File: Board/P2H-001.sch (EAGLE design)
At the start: 28 parts, among them IC1 74LS157N, IC2 LTC485N, IC3 4051N, IC4 74LS07N, IC5 LTC485N

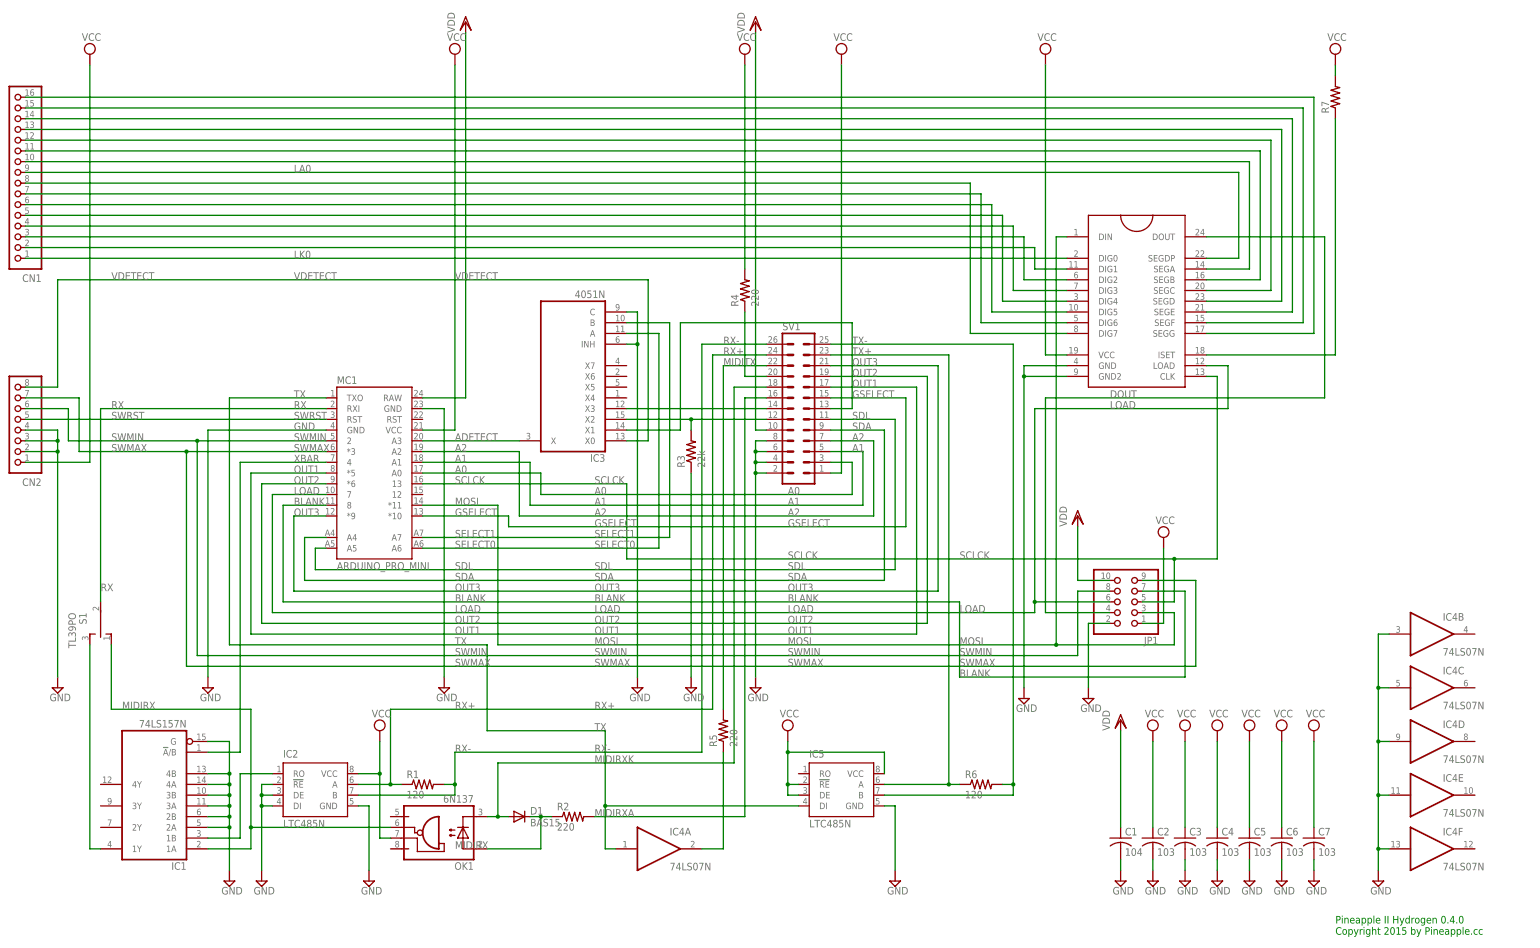
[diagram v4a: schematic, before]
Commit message: New drive port.
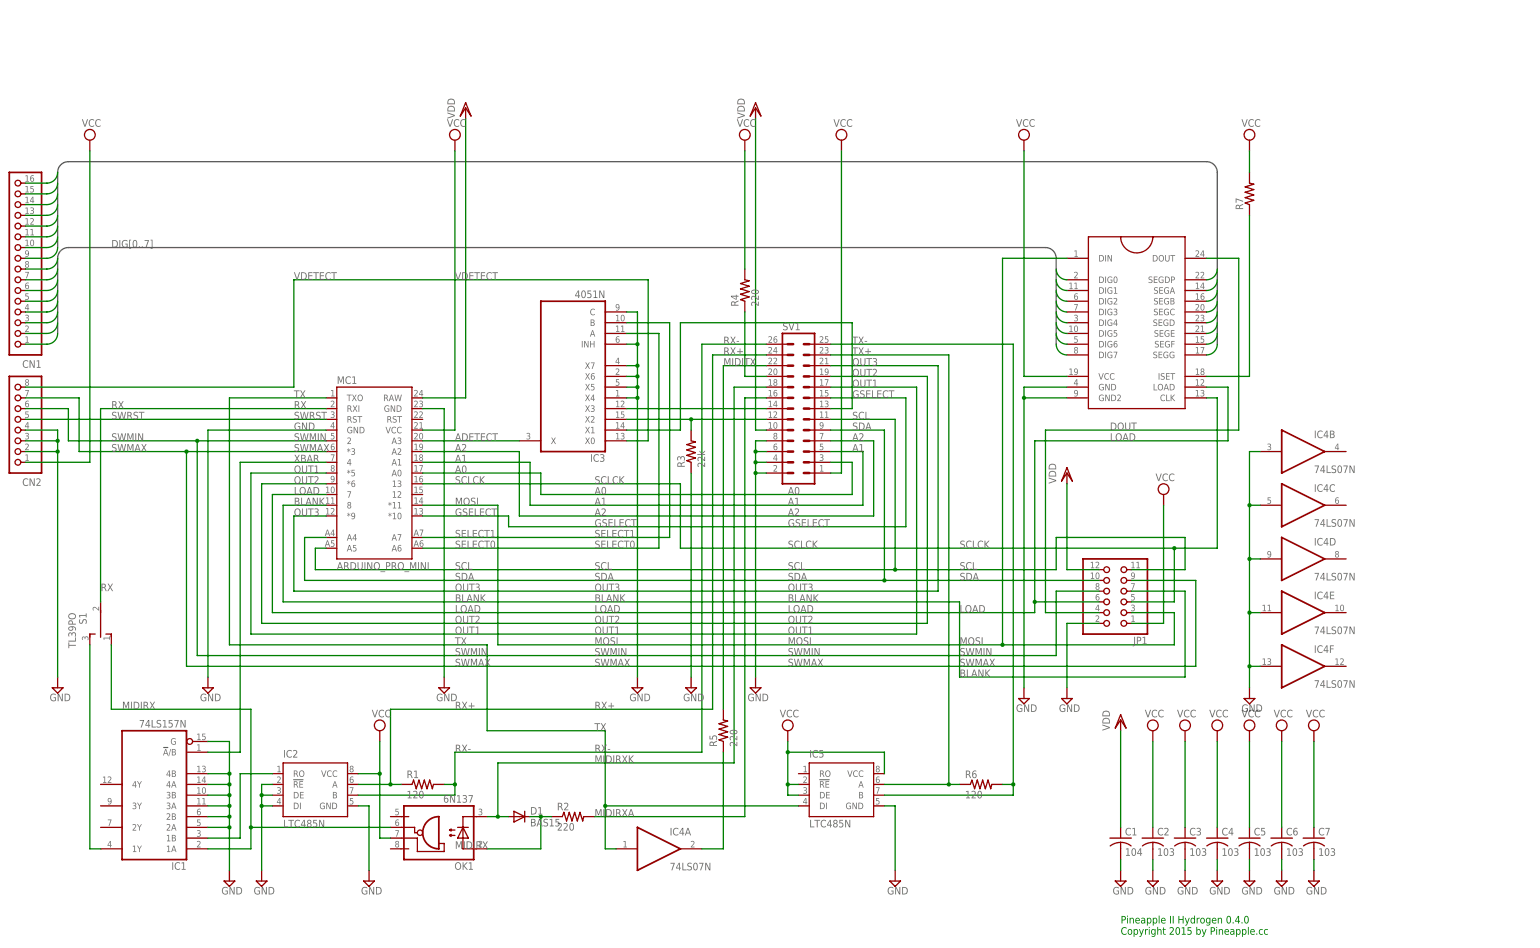
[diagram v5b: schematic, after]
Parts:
- JP1: device pinhead:PINHD-2X5 -> pinhead:PINHD-2X6
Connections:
- net LK0 renamed DIG0
- net N$18 renamed DIG2
- net N$19 renamed DIG3
- net N$22 renamed DIG1
- net N$24 renamed DIG4
- net N$25 renamed DIG5
- net N$26 renamed DIG6
- net N$27 renamed DIG7
- removed net LA0: CN1.9, MC2.SEGDP
- removed net N$29: CN1.10, MC2.SEGA
- removed net N$30: CN1.11, MC2.SEGB
- removed net N$31: CN1.12, MC2.SEGC
- removed net N$32: CN1.13, MC2.SEGD
- removed net N$33: CN1.14, MC2.SEGE
- removed net N$34: CN1.15, MC2.SEGF
- removed net N$35: CN1.16, MC2.SEGG
- removed net SDL: MC1.A5, SV1.11
- new net SCL: JP1.11, MC1.A5, SV1.11
- new net SEG0: CN1.9, MC2.SEGG
- new net SEG1: CN1.10, MC2.SEGF
- new net SEG2: CN1.11, MC2.SEGE
- new net SEG3: CN1.12, MC2.SEGD
- new net SEG4: CN1.13, MC2.SEGC
- new net SEG5: CN1.14, MC2.SEGB
- new net SEG6: CN1.15, MC2.SEGA
- new net SEG7: CN1.16, MC2.SEGDP
- net GND: now also IC3A.X4, IC3A.X5, IC3A.X6, IC3A.X7
- net SDA: now also JP1.10
- net VDD: now also JP1.12; no longer JP1.10
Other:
- moved on the sheet: CN1, IC4B, IC4C, IC4D, IC4E, IC4F, R7

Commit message: Updating...
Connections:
- net RX+: now also SV1.23; no longer SV1.24
- net RX-: now also SV1.24; no longer SV1.26
- net TX+: now also SV1.25; no longer SV1.23
- net TX-: now also SV1.26; no longer SV1.25
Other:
- moved on the sheet: R4
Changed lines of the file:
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@@
 <instances>
 <instance part="SUPPLY1" gate="GND" x="20.32" y="-22.86"/>
-<instance part="R4" gate="G$1" x="182.88" y="71.12" rot="R90"/>
+<instance part="R4" gate="G$1" x="182.88" y="73.66" rot="R90"/>
 <instance part="R5" gate="G$1" x="177.8" y="-33.02" rot="R90"/>
 <instance part="R2" gate="G$1" x="142.24" y="-53.34"/>
@@
 <pinref part="SUPPLY13" gate="G$1" pin="VCC"/>
 <pinref part="R4" gate="G$1" pin="2"/>
-<wire x1="182.88" y1="104.14" x2="182.88" y2="76.2" width="0.1524" layer="91"/>
+<wire x1="182.88" y1="104.14" x2="182.88" y2="78.74" width="0.1524" layer="91"/>
 </segment>
 <segment>
@@
 <wire x1="111.76" y1="-45.72" x2="114.3" y2="-45.72" width="0.1524" layer="91"/>
 <junction x="114.3" y="-45.72"/>
-<pinref part="SV1" gate="1" pin="26"/>
-<wire x1="187.96" y1="58.42" x2="172.72" y2="58.42" width="0.1524" layer="91"/>
-<wire x1="172.72" y1="58.42" x2="172.72" y2="-38.1" width="0.1524" layer="91"/>
+<wire x1="172.72" y1="55.88" x2="172.72" y2="-38.1" width="0.1524" layer="91"/>
 <wire x1="172.72" y1="-38.1" x2="114.3" y2="-38.1" width="0.1524" layer="91"/>
 <wire x1="114.3" y1="-38.1" x2="114.3" y2="-45.72" width="0.1524" layer="91"/>
 <label x="114.3" y="-38.1" size="1.778" layer="95"/>
 <label x="147.32" y="-38.1" size="1.778" layer="95"/>
-<label x="177.8" y="58.42" size="1.778" layer="95"/>
+<pinref part="SV1" gate="1" pin="24"/>
+<wire x1="172.72" y1="55.88" x2="187.96" y2="55.88" width="0.1524" layer="91"/>
+<label x="180.34" y="55.88" size="1.778" layer="95"/>
 </segment>
 </net>
@@
 <wire x1="91.44" y1="-45.72" x2="99.06" y2="-45.72" width="0.1524" layer="91"/>
 <wire x1="99.06" y1="-27.94" x2="99.06" y2="-45.72" width="0.1524" layer="91"/>
-<pinref part="SV1" gate="1" pin="24"/>
-<wire x1="187.96" y1="55.88" x2="175.26" y2="55.88" width="0.1524" layer="91"/>
-<wire x1="175.26" y1="55.88" x2="175.26" y2="-27.94" width="0.1524" layer="91"/>
-<wire x1="175.26" y1="-27.94" x2="99.06" y2="-27.94" width="0.1524" layer="91"/>
+<wire x1="233.68" y1="55.88" x2="233.68" y2="-27.94" width="0.1524" layer="91"/>
+<wire x1="233.68" y1="-27.94" x2="99.06" y2="-27.94" width="0.1524" layer="91"/>
 <pinref part="R1" gate="G$1" pin="1"/>
 <wire x1="101.6" y1="-45.72" x2="99.06" y2="-45.72" width="0.1524" layer="91"/>
@@
 <label x="147.32" y="-27.94" size="1.778" layer="95"/>
 <label x="114.3" y="-27.94" size="1.778" layer="95"/>
-<label x="177.8" y="55.88" size="1.778" layer="95"/>
+<pinref part="SV1" gate="1" pin="23"/>
+<wire x1="233.68" y1="55.88" x2="203.2" y2="55.88" width="0.1524" layer="91"/>
+<label x="208.28" y="55.88" size="1.778" layer="95"/>
 </segment>
 </net>
@@
 <pinref part="R6" gate="G$1" pin="1"/>
 <wire x1="215.9" y1="-45.72" x2="231.14" y2="-45.72" width="0.1524" layer="91"/>
-<pinref part="SV1" gate="1" pin="23"/>
 <wire x1="231.14" y1="-45.72" x2="233.68" y2="-45.72" width="0.1524" layer="91"/>
-<wire x1="203.2" y1="55.88" x2="231.14" y2="55.88" width="0.1524" layer="91"/>
-<wire x1="231.14" y1="55.88" x2="231.14" y2="-45.72" width="0.1524" layer="91"/>
+<wire x1="231.14" y1="58.42" x2="231.14" y2="-45.72" width="0.1524" layer="91"/>
 <junction x="231.14" y="-45.72"/>
-<label x="208.28" y="55.88" size="1.778" layer="95"/>
+<pinref part="SV1" gate="1" pin="25"/>
+<wire x1="231.14" y1="58.42" x2="203.2" y2="58.42" width="0.1524" layer="91"/>
+<label x="208.28" y="58.42" size="1.778" layer="95"/>
 </segment>
 </net>
@@
 <wire x1="246.38" y1="-48.26" x2="246.38" y2="-45.72" width="0.1524" layer="91"/>
 <wire x1="246.38" y1="-45.72" x2="243.84" y2="-45.72" width="0.1524" layer="91"/>
-<pinref part="SV1" gate="1" pin="25"/>
-<wire x1="203.2" y1="58.42" x2="246.38" y2="58.42" width="0.1524" layer="91"/>
-<wire x1="246.38" y1="58.42" x2="246.38" y2="-45.72" width="0.1524" layer="91"/>
+<wire x1="246.38" y1="66.04" x2="246.38" y2="-45.72" width="0.1524" layer="91"/>
 <junction x="246.38" y="-45.72"/>
-<label x="208.28" y="58.42" size="1.778" layer="95"/>
+<wire x1="246.38" y1="66.04" x2="180.34" y2="66.04" width="0.1524" layer="91"/>
+<wire x1="180.34" y1="66.04" x2="180.34" y2="58.42" width="0.1524" layer="91"/>
+<pinref part="SV1" gate="1" pin="26"/>
+<wire x1="180.34" y1="58.42" x2="187.96" y2="58.42" width="0.1524" layer="91"/>
+<label x="180.34" y="58.42" size="1.778" layer="95"/>
 </segment>
 </net>
@@
 <wire x1="83.82" y1="20.32" x2="73.66" y2="20.32" width="0.1524" layer="91"/>
 <wire x1="73.66" y1="20.32" x2="73.66" y2="-2.54" width="0.1524" layer="91"/>
-<wire x1="73.66" y1="-2.54" x2="233.68" y2="-2.54" width="0.1524" layer="91"/>
+<wire x1="73.66" y1="-2.54" x2="241.3" y2="-2.54" width="0.1524" layer="91"/>
 <label x="114.3" y="-2.54" size="1.778" layer="95"/>
 <label x="76.2" y="20.32" size="1.778" layer="95"/>
-<wire x1="233.68" y1="-2.54" x2="233.68" y2="-20.32" width="0.1524" layer="91"/>
-<wire x1="233.68" y1="-20.32" x2="287.02" y2="-20.32" width="0.1524" layer="91"/>
+<wire x1="241.3" y1="-2.54" x2="241.3" y2="-20.32" width="0.1524" layer="91"/>
+<wire x1="241.3" y1="-20.32" x2="287.02" y2="-20.32" width="0.1524" layer="91"/>
 <wire x1="287.02" y1="-20.32" x2="287.02" y2="0" width="0.1524" layer="91"/>
 <wire x1="287.02" y1="0" x2="274.32" y2="0" width="0.1524" layer="91"/>
@@
 <segment>
 <pinref part="R4" gate="G$1" pin="1"/>
-<wire x1="182.88" y1="66.04" x2="182.88" y2="50.8" width="0.1524" layer="91"/>
+<wire x1="182.88" y1="68.58" x2="182.88" y2="50.8" width="0.1524" layer="91"/>
 <pinref part="SV1" gate="1" pin="20"/>
 <wire x1="182.88" y1="50.8" x2="187.96" y2="50.8" width="0.1524" layer="91"/>
@@
 <wire x1="177.8" y1="53.34" x2="177.8" y2="-27.94" width="0.1524" layer="91"/>
 <pinref part="R5" gate="G$1" pin="2"/>
-<label x="177.8" y="53.34" size="1.778" layer="95"/>
-</segment>
-</net>
+<label x="180.34" y="53.34" size="1.778" layer="95"/>
+</segment>
+</net>

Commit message: Refine of sch.
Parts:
- removed JP1: (no value), pinhead:PINHD-2X6
- removed MC1: ARDUINO_PRO_MINI, SparkFun-Boards:ARDUINO_PRO_MINI
- removed MC2: MAX7219DIP, SparkFun-DigitalIC:MAX7219DIP
- added U1: ARDUINO_PRO_MINI, SparkFun-Boards:ARDUINO_PRO_MINI
- added U2: MAX7219DIP, SparkFun-DigitalIC:MAX7219DIP
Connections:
- removed net BLANK: JP1.7, MC1.8
- removed net DOUT: JP1.4, MC2.DOUT
- removed net MIDIRXA: R2.2, SV1.16
- removed net MIDIRXK: D1.A, OK1.C, SV1.18
- removed net MIDITX: R5.2, SV1.22
- removed net N$3: IC3A.X1, SV1.13
- removed net N$5: IC3A.X2, R3.2, SV1.12
- removed net N$6: IC3A.X3, SV1.14
- removed net OUT1: MC1.*5, SV1.17
- removed net OUT2: MC1.*6, SV1.19
- removed net OUT3: MC1.*9, SV1.21
- removed net SELECT0: IC3A.A, MC1.A6
- removed net SELECT1: IC3A.B, MC1.A7
- removed net SWRST: CN2.5, MC1.RST
- new net GDETECT: IC3A.X1, SV1.11
- new net L0: SV1.13, U1.*5
- new net L1: SV1.14, U1.*6
- new net L2: SV1.15, U1.*9
- new net MDETECT: IC3A.X2, R3.2, SV1.16
- new net RXA: R2.2, SV1.19
- new net RXK: D1.A, OK1.C, SV1.20
- new net SEL0: IC3A.A, U1.A6
- new net SEL1: IC3A.B, U1.A7
- new net SWMAIN: CN2.3, U1.2
- new net TXSNK: R4.2, SV1.18
- new net XDETECT: IC3A.X3, SV1.22
- net A0: now also U1.A0; no longer MC1.A0
- net A1: now also U1.A1; no longer MC1.A1
- net A2: now also U1.A2; no longer MC1.A2
- net ADETECT: now also U1.A3; no longer MC1.A3
- net DIG0: now also U2.DIG0; no longer MC2.DIG0
- net DIG1: now also U2.DIG1; no longer MC2.DIG1
- net DIG2: now also U2.DIG2; no longer MC2.DIG2
- net DIG3: now also U2.DIG3; no longer MC2.DIG3
- net DIG4: now also U2.DIG4; no longer MC2.DIG4
- net DIG5: now also U2.DIG5; no longer MC2.DIG5
- net DIG6: now also U2.DIG6; no longer MC2.DIG6
- net DIG7: now also U2.DIG7; no longer MC2.DIG7
- net GND: now also U1.GND, U1.GND@2, U2.GND, U2.GND2; no longer CN2.3, CN2.4, JP1.2, MC1.GND, MC1.GND@2, MC2.GND, MC2.GND2, SV1.8
- net GSELECT: now also SV1.12, U1.*10; no longer MC1.*10, SV1.15
- net LOAD: now also SV1.21, U1.7, U2.LOAD; no longer JP1.6, MC1.7, MC2.LOAD
- net MOSI: now also CN2.6, U1.*11, U2.DIN; no longer JP1.3, MC1.*11, MC2.DIN
- net N$12: now also R5.1, SV1.17; no longer R4.1, SV1.20
- net N$2: now also R4.1; no longer R5.1
- net N$21: now also U2.ISET; no longer MC2.ISET
- net RX: now also U1.RXI; no longer MC1.RXI
- net SCL: now also SV1.10, U1.A5; no longer JP1.11, MC1.A5, SV1.11
- net SCLCK: now also CN2.7, U1.13, U2.CLK; no longer JP1.5, MC1.13, MC2.CLK
- net SDA: now also U1.A4; no longer JP1.10, MC1.A4
- net SEG0: now also U2.SEGG; no longer MC2.SEGG
- net SEG1: now also U2.SEGF; no longer MC2.SEGF
- net SEG2: now also U2.SEGE; no longer MC2.SEGE
- net SEG3: now also U2.SEGD; no longer MC2.SEGD
- net SEG4: now also U2.SEGC; no longer MC2.SEGC
- net SEG5: now also U2.SEGB; no longer MC2.SEGB
- net SEG6: now also U2.SEGA; no longer MC2.SEGA
- net SEG7: now also U2.SEGDP; no longer MC2.SEGDP
- net SWMAX: now also CN2.4, U1.*3; no longer CN2.7, JP1.9, MC1.*3
- net SWMIN: now also CN2.5, U1.4; no longer CN2.6, JP1.8, MC1.2
- net TX: now also U1.TXO; no longer MC1.TXO
- net VCC: now also R5.2, U1.VCC, U2.VCC; no longer JP1.1, MC1.VCC, MC2.VCC, R4.2
- net VDD: now also SV1.8, U1.RAW; no longer JP1.12, MC1.RAW, SV1.10
- net XBAR: now also U1.8; no longer MC1.4
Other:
- moved on the sheet: C1, C2, C3, C4, C5, C6, C7, D1, IC2, IC3, IC4A, IC4B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

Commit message: fine tuning.
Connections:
- net MOSI renamed S0
- net RX+ renamed M0
- net RX- renamed M1
- net SCLCK renamed S1
- net SDA renamed I2C0
- net TX+ renamed M2
- net TX- renamed M3
- removed net LOAD: SV1.21, U1.7, U2.LOAD
- removed net N$12: R5.1, SV1.17
- removed net SCL: SV1.10, U1.A5
- new net I2C1: SV1.11, U1.A5
- new net N$3: R5.1, SV1.21
- new net S2: U1.7, U2.LOAD
- net GDETECT: now also SV1.12; no longer SV1.11
- net GND: now also SV1.8
- net GSELECT: now also SV1.13; no longer SV1.12
- net L0: now also SV1.14; no longer SV1.13
- net L1: now also SV1.15; no longer SV1.14
- net L2: now also SV1.16; no longer SV1.15
- net MDETECT: now also SV1.17; no longer SV1.16
- net TXSNK: now also SV1.22; no longer SV1.18
- net VDD: now also SV1.10; no longer SV1.8
- net XDETECT: now also SV1.18; no longer SV1.22
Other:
- moved on the sheet: IC4A, R3, R4, R5, R6, R7, S1
